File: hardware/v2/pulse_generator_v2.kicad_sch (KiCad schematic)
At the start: 27 parts, among them J1 Power, J2 Digital/PWM, J3 Analog, J4 Digital/PWM, J5 Conn_Coaxial, J6 Conn_Coaxial, SW1 SW_Push, U1 LM311, U2 74LS279

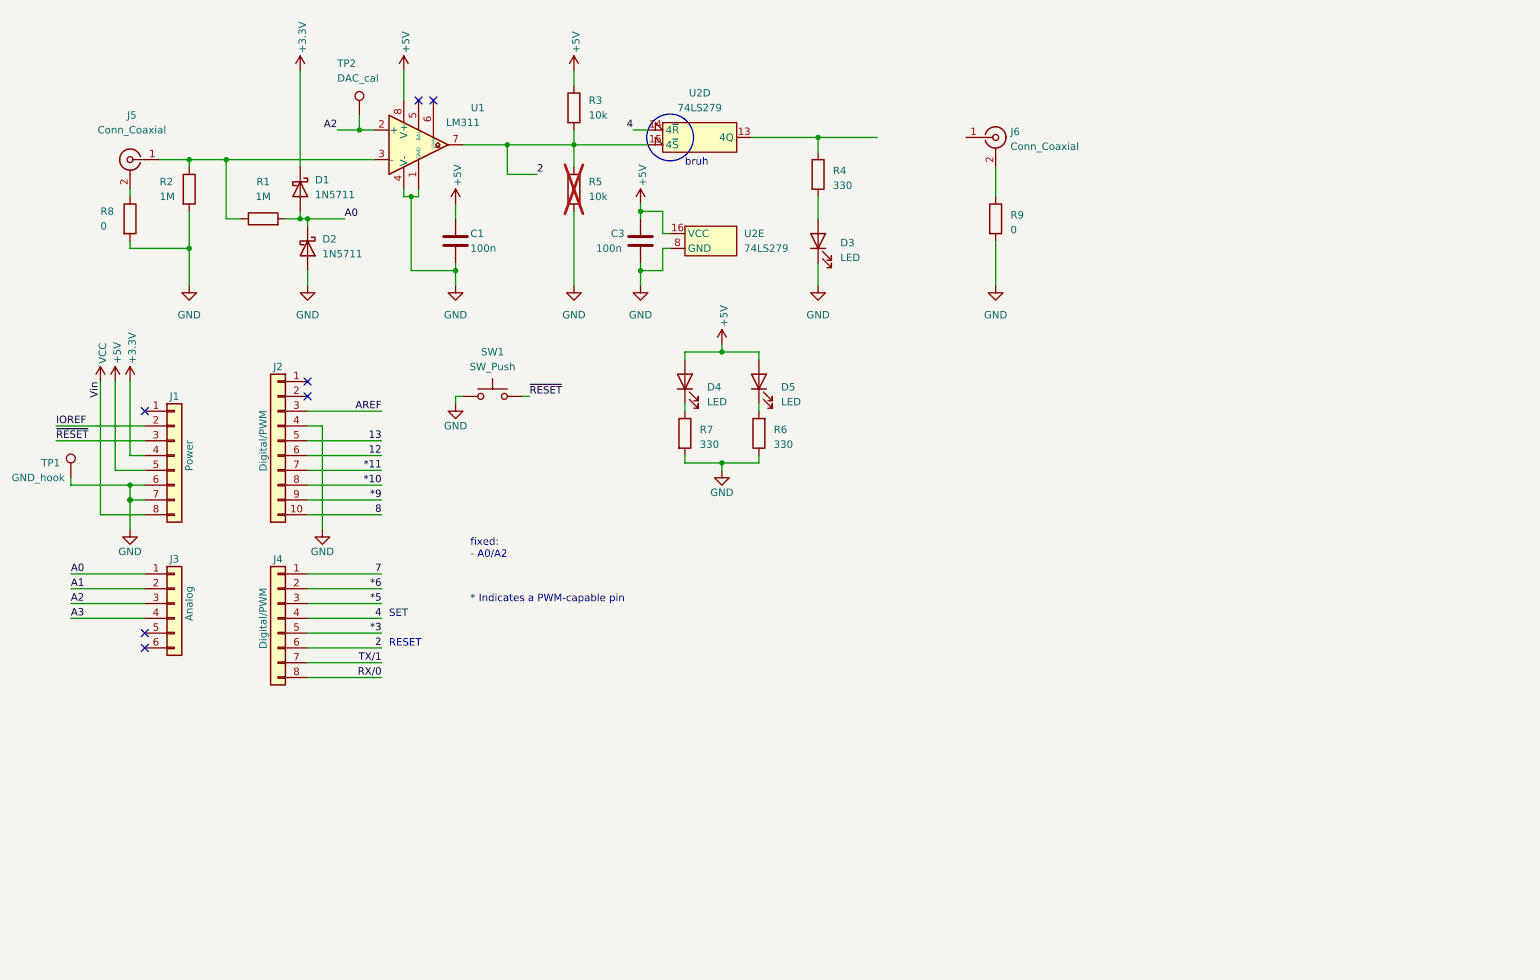
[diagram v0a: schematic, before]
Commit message: added pdf of v2 w relay circuit
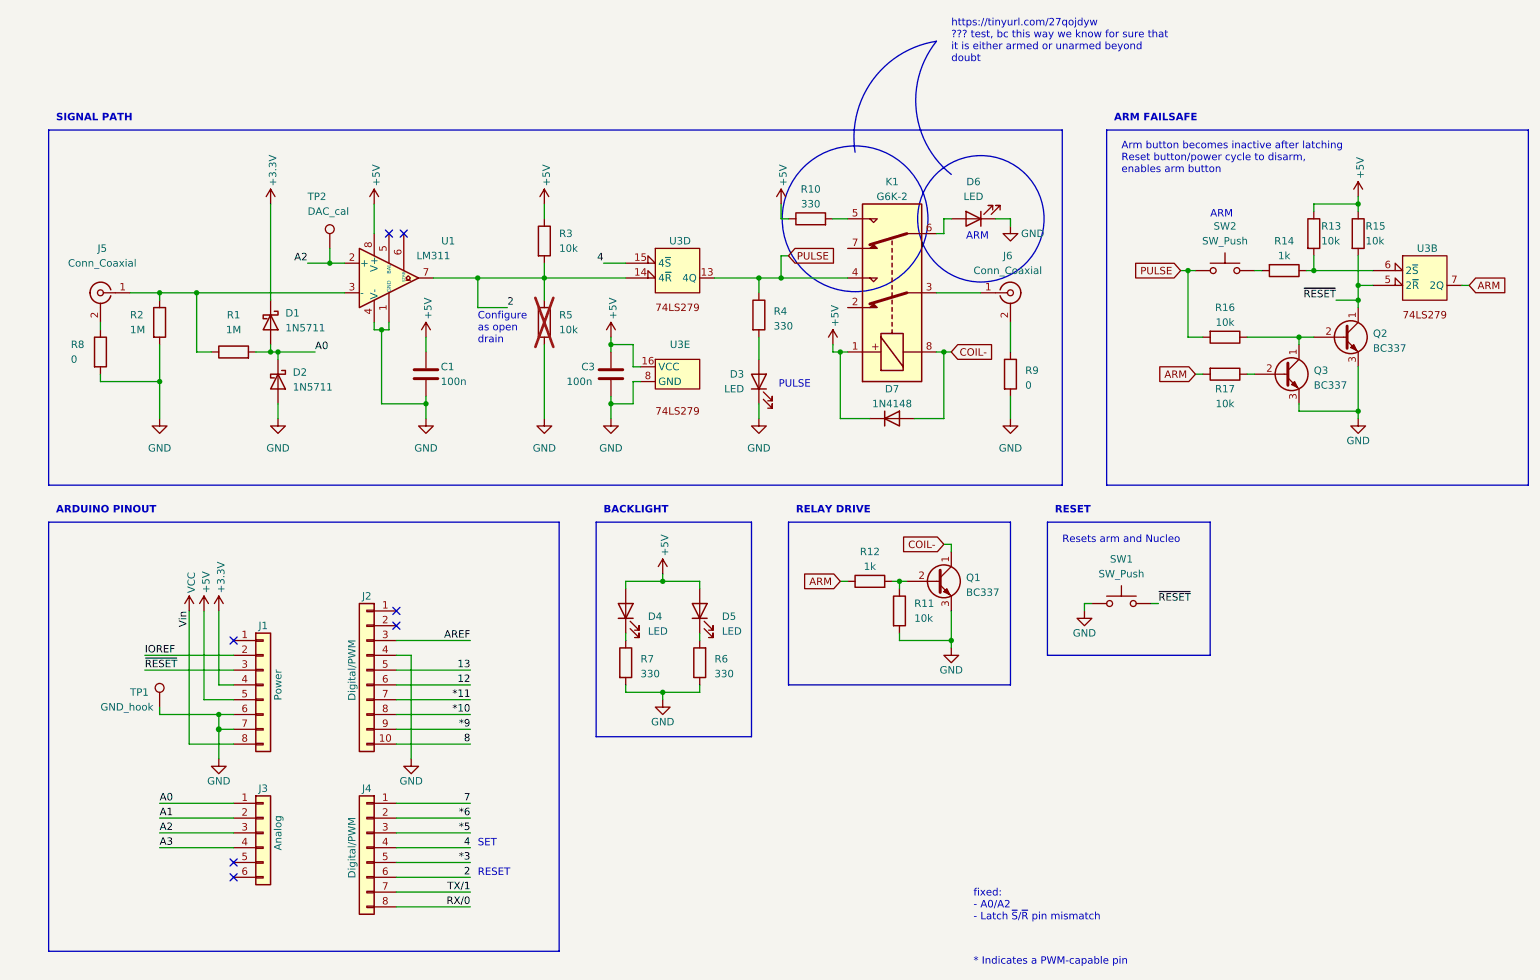
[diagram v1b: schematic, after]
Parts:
- removed U2: 74LS279, Package_DIP:DIP-16_W7.62mm_Socket_LongPads, symbol comprovat_parts:74LS279
- added D6: LED, LED_THT:LED_D5.0mm, symbol Device:LED
- added D7: 1N4148, Diode_THT:D_DO-35_SOD27_P7.62mm_Horizontal, symbol Diode:1N4148
- added K1: G6K-2, Relay_SMD:Relay_DPDT_Omron_G6K-2F-Y, symbol Relay:G6K-2
- added Q1, Q2, Q3: BC337, Package_TO_SOT_THT:TO-92_Inline, symbol Transistor_BJT:BC337
- added R10: 330, Resistor_SMD:R_0805_2012Metric_Pad1.20x1.40mm_HandSolder, symbol Device:R
- added R11, R13, R15, R16, R17: 10k, Resistor_SMD:R_0805_2012Metric_Pad1.20x1.40mm_HandSolder, symbol Device:R
- added R12, R14: 1k, Resistor_SMD:R_0805_2012Metric_Pad1.20x1.40mm_HandSolder, symbol Device:R
- added SW2: SW_Push, Button_Switch_THT:SW_Tactile_SPST_Angled_PTS645Vx39-2LFS, symbol Switch:SW_Push
- added U3: ~, symbol guillem_symbols:74LS279
- D4, D5: footprint LED_SMD:LED_0805_2012Metric_Pad1.15x1.40mm_HandSolder -> LED_THT:LED_D5.0mm
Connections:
- net +5V: now also D7.1 (K), K1.1, R10.1, R13.1, R15.1, U3.16 (VCC)
- net 2: now also U3.14 (4~{R})
- net 4: now also U3.15 (4~{S})
- net GND: now also D6.1 (K), Q1.3 (E), Q2.3 (E), Q3.3 (E), R11.2, U3.8 (GND)
- net ~{RESET}: now also Q2.1 (C), R15.2, U3.5 (2~{R})
- net at J6.1 (In): now also K1.3
- net PULSE: now reaches R4.1
- net PULSE: now also K1.4, R16.2, SW2.1, U3.13 (4Q)
- new net: Q2.2 (B), Q3.1 (C), R16.1
- new net: Q3.2 (B), R17.1
- new net: R13.2, R14.1, U3.6 (2~{S})
- new net: R14.2, SW2.2
- new net: D6.2 (A), K1.6
- new net: Q1.2 (B), R11.1, R12.2
- new net: K1.5, R10.2
- new net ARM: R12.1, R17.2, U3.7 (2Q)
- new net COIL-: D7.2 (A), K1.8, Q1.1 (C)
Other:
- note added: "ARDUINO PINOUT"
- note added: "ARM"
- note added: "ARM FAILSAFE"
- note added: "Arm button becomes inactive after latching Reset button/power cycle to disarm, enables arm button"
- note added: "BACKLIGHT"
- note added: "Configure as open drain"
- note added: "PULSE"
- note added: "RELAY DRIVE"
- note added: "Resets arm and Nucleo"
- note added: "SIGNAL PATH"
- note added: "fixed: - A0/A2 - Latch ~{S}/~{R} pin mismatch"
- note added: "https://tinyurl.com/27qojdyw ??? test, bc this way we know for sure that it is either armed or unarmed beyond doubt"
- note removed: "bruh"
- note removed: "fixed: - A0/A2"
- moved on the sheet: C1, C3, D1, D2, D3, D4, D5, J1, J2, J3, J4, J5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

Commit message: failsafe arm fixes
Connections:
- net +5V: now also R10.2; no longer R10.1
- net GND: no longer D6.1 (K)
- net at D6.2 (A): now also R10.1; no longer K1.6
- net at K1.5: no longer R10.2
- net at J6.1 (In), K1.3: now also D6.1 (K)
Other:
- note added: "*1"
- note added: "*1: DPST due to availability"
- note added: "ARMED"
- note added: "PULSING"
- note removed: "PULSE"
- note removed: "https://tinyurl.com/27qojdyw ??? test, bc this way we know for sure that it is either armed or unarmed beyond doubt"
- moved on the sheet: D6, R10
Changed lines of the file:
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@@
   (junction (at 142.24 62.23) (diameter 0) (color 0 0 0 0)
+  )
+  (junction (at 176.53 64.77) (diameter 0) (color 0 0 0 0)
   )
   (junction (at 49.53 139.7) (diameter 1.016) (color 0 0 0 0)
@@
     (stroke (width 0) (type default))
   )
-  (wire (pts (xy 146.05 52.07) (xy 147.32 52.07))
-    (stroke (width 0) (type default))
-  )
   (wire (pts (xy 132.08 123.19) (xy 132.08 124.46))
     (stroke (width 0) (type default))
@@
     (stroke (width 0) (type solid))
   )
-  (wire (pts (xy 173.99 52.07) (xy 175.26 52.07))
-    (stroke (width 0) (type default))
-  )
   (wire (pts (xy 49.53 132.08) (xy 52.07 132.08))
     (stroke (width 0) (type solid))
@@
     (stroke (width 0) (type solid))
   )
-  (wire (pts (xy 185.42 53.34) (xy 185.42 52.07))
-    (stroke (width 0) (type default))
-  )
   (wire (pts (xy 86.36 62.23) (xy 93.98 62.23))
     (stroke (width 0) (type default))
@@
     (stroke (width 0) (type default))
   )
+  (wire (pts (xy 176.53 54.61) (xy 176.53 55.88))
+    (stroke (width 0) (type default))
+  )
   (wire (pts (xy 175.26 124.46) (xy 175.26 125.73))
     (stroke (width 0) (type default))
@@
     (stroke (width 0) (type default))
   )
-  (wire (pts (xy 173.99 54.61) (xy 173.99 52.07))
-    (stroke (width 0) (type default))
-  )
   (wire (pts (xy 121.92 77.47) (xy 120.65 77.47))
     (stroke (width 0) (type default))
@@
     (stroke (width 0) (type default))
   )
-  (wire (pts (xy 172.72 54.61) (xy 173.99 54.61))
-    (stroke (width 0) (type default))
-  )
   (wire (pts (xy 78.74 69.85) (xy 78.74 71.12))
     (stroke (width 0) (type default))
@@
     (stroke (width 0) (type default))
   )
-  (wire (pts (xy 146.05 49.53) (xy 146.05 52.07))
-    (stroke (width 0) (type default))
-  )
-  (wire (pts (xy 172.72 64.77) (xy 180.34 64.77))
+  (wire (pts (xy 176.53 63.5) (xy 176.53 64.77))
+    (stroke (width 0) (type default))
+  )
+  (wire (pts (xy 172.72 64.77) (xy 176.53 64.77))
     (stroke (width 0) (type default))
   )
@@
     (stroke (width 0) (type solid))
   )
+  (wire (pts (xy 176.53 45.72) (xy 176.53 46.99))
+    (stroke (width 0) (type default))
+  )
   (wire (pts (xy 142.24 62.23) (xy 142.24 64.77))
     (stroke (width 0) (type default))
@@
     (stroke (width 0) (type default))
   )
-  (wire (pts (xy 182.88 52.07) (xy 185.42 52.07))
-    (stroke (width 0) (type default))
-  )
   (wire (pts (xy 237.49 60.96) (xy 247.65 60.96))
     (stroke (width 0) (type default))
@@
     (stroke (width 0) (type default))
   )
-  (wire (pts (xy 154.94 52.07) (xy 157.48 52.07))
+  (wire (pts (xy 176.53 64.77) (xy 180.34 64.77))
     (stroke (width 0) (type default))
   )
@@
     (stroke (width 0) (type solid))
   )
-  (arc (start 158.75 40.64) (mid 161.7896 28.2217) (end 172.72 21.59)
+  (rectangle (start 201.93 36.83) (end 274.32 97.79)
     (stroke (width 0) (type default))
     (fill (type none))
   )
-  (circle (center 180.34 52.07) (radius 10.8509)
+  (rectangle (start 20.32 36.83) (end 194.31 97.79)
     (stroke (width 0) (type default))
     (fill (type none))
   )
-  (rectangle (start 201.93 36.83) (end 274.32 97.79)
+  (rectangle (start 20.32 104.14) (end 107.95 177.8)
     (stroke (width 0) (type default))
     (fill (type none))
   )
-  (rectangle (start 20.32 36.83) (end 194.31 97.79)
+  (rectangle (start 114.3 104.14) (end 140.97 140.97)
     (stroke (width 0) (type default))
     (fill (type none))
   )
-  (circle (center 158.75 52.07) (radius 12.508)
+  (rectangle (start 147.32 104.14) (end 185.42 132.08)
     (stroke (width 0) (type default))
     (fill (type none))
   )
-  (rectangle (start 20.32 104.14) (end 107.95 177.8)
+  (rectangle (start 191.77 104.14) (end 219.71 127)
     (stroke (width 0) (type default))
     (fill (type none))
   )
-  (rectangle (start 114.3 104.14) (end 140.97 140.97)
-    (stroke (width 0) (type default))
-    (fill (type none))
-  )
-  (arc (start 175.26 44.45) (mid 169.2555 33.5461) (end 172.72 21.59)
-    (stroke (width 0) (type default))
-    (fill (type none))
-  )
-  (rectangle (start 147.32 104.14) (end 185.42 132.08)
-    (stroke (width 0) (type default))
-    (fill (type none))
-  )
-  (rectangle (start 191.77 104.14) (end 219.71 127)
-    (stroke (width 0) (type default))
-    (fill (type none))
-  )
   (text "ARM" (at 219.71 52.07 0)
     (effects (font (size 1.27 1.27)) (justify left bottom))
   )
-  (text "ARM" (at 177.8 55.88 0)
+  (text "ARMED" (at 177.8 57.15 0)
     (effects (font (size 1.27 1.27)) (justify left bottom))
   )
@@
     (effects (font (size 1.27 1.27)) (justify left bottom))
   )
-  (text "https://tinyurl.com/27qojdyw\n??? test, bc this way we know for sure that\nit is either armed or unarmed beyond\ndoubt"
-    (at 175.26 25.4 0)
+  (text "*1" (at 168.91 46.99 0)
     (effects (font (size 1.27 1.27)) (justify left bottom))
   )
@@
     (effects (font (size 1.27 1.27) (thickness 0.254) bold) (justify left bottom))
   )
+  (text "*1: DPST due to availability" (at 179.07 175.26 0)
+    (effects (font (size 1.27 1.27)) (justify left bottom))
+  )
   (text "RELAY DRIVE" (at 148.59 102.87 0)
     (effects (font (size 1.27 1.27) (thickness 0.254) bold) (justify left bottom))
@@
     (effects (font (size 1.27 1.27)) (justify left bottom))
   )
-  (text "PULSE" (at 151.13 81.28 0)
+  (text "PULSING" (at 152.4 81.28 0)
     (effects (font (size 1.27 1.27)) (justify right bottom))
   )
@@
     )
   )
-  (symbol (lib_id "power:+5V") (at 146.05 49.53 0) (unit 1)
-    (in_bom yes) (on_board yes) (dnp no)
-    (property "Reference" "#PWR021" (at 146.05 53.34 0)
-      (effects (font (size 1.27 1.27)) hide)
-    )
-    (property "Value" "+5V" (at 146.4056 46.482 90)
-      (effects (font (size 1.27 1.27)) (justify left))
-    )
-    (property "Footprint" "" (at 146.05 49.53 0)
-      (effects (font (size 1.27 1.27)))
-    )
-    (property "Datasheet" "" (at 146.05 49.53 0)
+  (symbol (lib_id "power:+5V") (at 176.53 45.72 0) (unit 1)
+    (in_bom yes) (on_board yes) (dnp no)
+    (property "Reference" "#PWR021" (at 176.53 49.53 0)
+      (effects (font (size 1.27 1.27)) hide)
+    )
+    (property "Value" "+5V" (at 176.8856 42.672 90)
+      (effects (font (size 1.27 1.27)) (justify left))
+    )
+    (property "Footprint" "" (at 176.53 45.72 0)
+      (effects (font (size 1.27 1.27)))
+    )
+    (property "Datasheet" "" (at 176.53 45.72 0)
       (effects (font (size 1.27 1.27)))
     )
@@
     )
   )
-  (symbol (lib_id "power:GND") (at 185.42 53.34 0) (unit 1)
-    (in_bom yes) (on_board yes) (dnp no)
-    (property "Reference" "#PWR06" (at 185.42 59.69 0)
-      (effects (font (size 1.27 1.27)) hide)
-    )
-    (property "Value" "GND" (at 189.23 54.61 0)
-      (effects (font (size 1.27 1.27)))
-    )
-    (property "Footprint" "" (at 185.42 53.34 0)
-      (effects (font (size 1.27 1.27)) hide)
-    )
-    (property "Datasheet" "" (at 185.42 53.34 0)
-      (effects (font (size 1.27 1.27)) hide)
-    )
-    (pin "1")
-    (instances
-      (project "pulse_generator_v2"
-        (path "/e63e39d7-6ac0-4ffd-8aa3-1841a4541b55"
-          (reference "#PWR06") (unit 1)
-        )
-      )
-    )
-  )
-  (symbol (lib_id "Device:LED") (at 179.07 52.07 180) (unit 1)
-    (in_bom yes) (on_board yes) (dnp no)
-    (property "Reference" "D6" (at 179.07 45.72 0)
-      (effects (font (size 1.27 1.27)))
-    )
-    (property "Value" "LED" (at 179.07 48.26 0)
-      (effects (font (size 1.27 1.27)))
-    )
-    (property "Footprint" "LED_THT:LED_D5.0mm" (at 179.07 52.07 0)
-      (effects (font (size 1.27 1.27)) hide)
-    )
-    (property "Datasheet" "~" (at 179.07 52.07 0)
+  (symbol (lib_id "Device:LED") (at 176.53 59.69 90) (unit 1)
+    (in_bom yes) (on_board yes) (dnp no)
+    (property "Reference" "D6" (at 172.72 60.96 90)
+      (effects (font (size 1.27 1.27)))
+    )
+    (property "Value" "LED" (at 172.72 58.42 90)
+      (effects (font (size 1.27 1.27)))
+    )
+    (property "Footprint" "LED_THT:LED_D5.0mm" (at 176.53 59.69 0)
+      (effects (font (size 1.27 1.27)) hide)
+    )
+    (property "Datasheet" "~" (at 176.53 59.69 0)
       (effects (font (size 1.27 1.27)) hide)
     )
@@
     )
   )
-  (symbol (lib_id "Device:R") (at 151.13 52.07 90) (unit 1)
+  (symbol (lib_id "Device:R") (at 176.53 50.8 180) (unit 1)
     (in_bom yes) (on_board yes) (dnp no) (fields_autoplaced)
-    (property "Reference" "R10" (at 151.13 46.99 90)
-      (effects (font (size 1.27 1.27)))
-    )
-    (property "Value" "330" (at 151.13 49.53 90)
-      (effects (font (size 1.27 1.27)))
-    )
-    (property "Footprint" "Resistor_SMD:R_0805_2012Metric_Pad1.20x1.40mm_HandSolder" (at 151.13 53.848 90)
-      (effects (font (size 1.27 1.27)) hide)
-    )
-    (property "Datasheet" "~" (at 151.13 52.07 0)
-      (effects (font (size 1.27 1.27)) hide)
-    )
+    (property "Reference" "R10" (at 179.07 50.165 0)
+      (effects (font (size 1.27 1.27)) (justify right))
+    )
+    (property "Value" "330" (at 179.07 52.705 0)
+      (effects (font (size 1.27 1.27)) (justify right))
+    )
+    (property "Footprint" "Resistor_SMD:R_0805_2012Metric_Pad1.20x1.40mm_HandSolder" (at 178.308 50.8 90)
+      (effects (font (size 1.27 1.27)) hide)
+    )
+    (property "Datasheet" "~" (at 176.53 50.8 0)
+      (effects (font (size 1.27 1.27)) hide)
+    )
